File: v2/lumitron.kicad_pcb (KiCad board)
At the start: 2 copper layers, 40.6 x 78.7 mm, 11 parts

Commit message: track layout cleanup
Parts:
- moved BT2 1.40 mm to (101.6, 96.5)
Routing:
- net /f: track 46.0 -> 70.5 mm
- net /g: track 53.8 -> 67.1 mm
- net /d: track 13.5 -> 26.8 mm
- net /a: track 83.4 -> 91.3 mm
- net /b: track 70.9 -> 78.0 mm
- net /e: track 21.0 -> 18.4 mm
- net /c: track 27.2 -> 24.8 mm

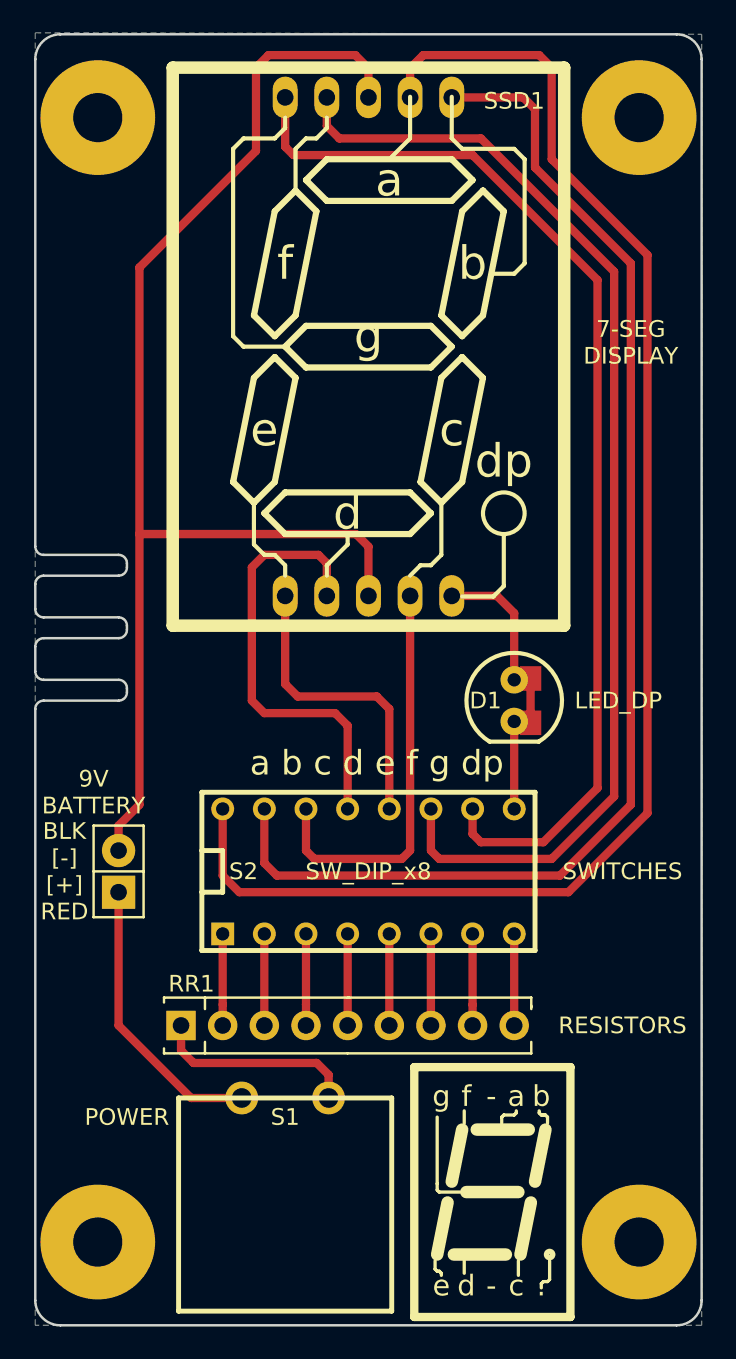
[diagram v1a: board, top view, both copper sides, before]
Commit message: added open source logo
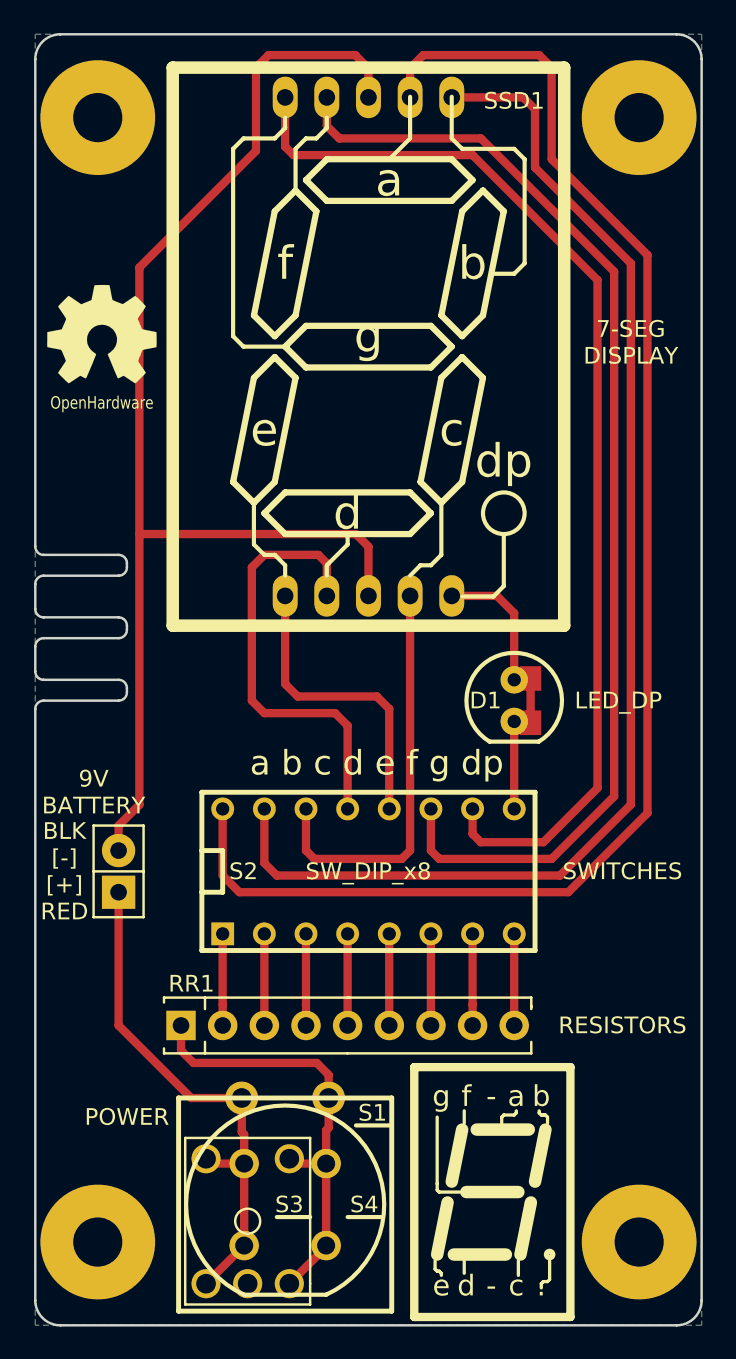
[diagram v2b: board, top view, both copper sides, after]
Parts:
- added G1: OSHW, lumitron_pcb:OSHW_6mm, F.Cu at (85.3, 94.5)
- added S3: POWER3, lumitron_pcb:sw_KSA_Tactile_SPST, F.Cu at (94.2, 148.6)
- added S4: POWER2, lumitron_pcb:sw_KS-01Q, F.Cu at (96.5, 147.6)
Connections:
- net Net-(RR1-Pad1) renamed /RES
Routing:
- net /[+]: track 17.5 -> 32.3 mm
- net /RES: track 12.6 -> 27.2 mm

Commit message: last cleanup before prototype
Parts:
- moved S3 0.25 mm to (94.2, 148.8)
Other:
- board text removed: "-"

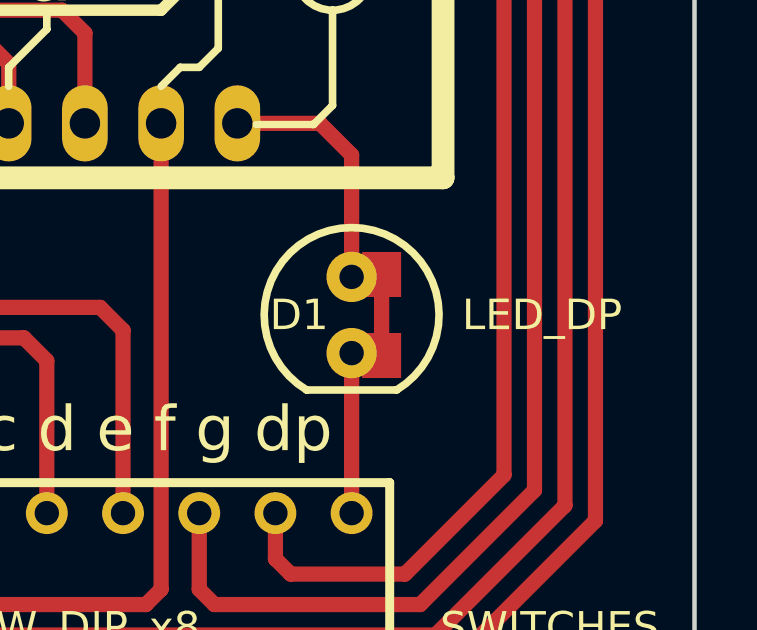
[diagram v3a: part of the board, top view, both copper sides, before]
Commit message: reverse LED DP D1 silk legend fixed
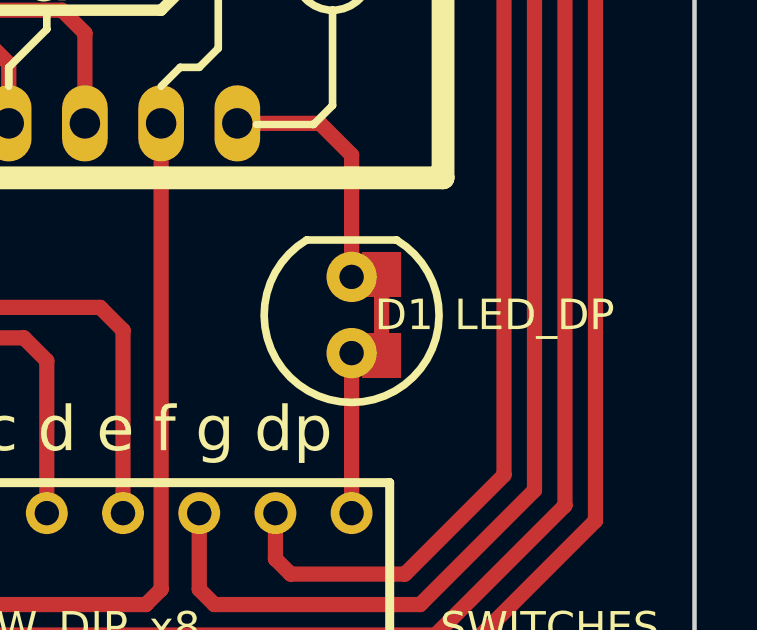
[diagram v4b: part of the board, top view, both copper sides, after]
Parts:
- turned D1 to 90 degrees
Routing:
- net /dp: track 18.4 -> 17.5 mm
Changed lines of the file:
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@@
     (thickness 1.6)
     (drawings 184)
-    (tracks 116)
+    (tracks 114)
     (zones 0)
     (modules 14)
@@
     (fp_text user [-] (at -10.16 1.27 180) (layer B.SilkS)
       (effects (font (size 1 1) (thickness 0.15)) (justify mirror))
-    )
-  )
-  (module lumitron_pcb:LED-5MM_SMD (layer F.Cu)
-    (at 110.49 116.84 270)
-    (descr "LED 5mm - Lead pitch 100mil (2,54mm)")
-    (tags "LED led 5mm 5MM 100mil 2,54mm")
-    (fp_text reference D1 (at 0 1.75 360) (layer F.SilkS)
-      (effects (font (size 1.016 1.016) (thickness 0.1524)))
-    )
-    (fp_text value LED_DP (at 0 -6.35 360) (layer F.SilkS)
-      (effects (font (size 1.016 1.016) (thickness 0.1524)))
-    )
-    (fp_arc (start 0 0) (end 2.5 1.5) (angle 298.0724869) (layer F.SilkS) (width 0.254))
-    (fp_line (start 2.5 -1.5) (end 2.5 1.5) (layer F.SilkS) (width 0.254))
-    (pad 1 thru_hole circle (at -1.27 0 270) (size 1.6764 1.6764) (drill 0.8128) (layers *.Cu *.Mask F.SilkS)
-      (net 9 /dp))
-    (pad 2 thru_hole circle (at 1.27 0 270) (size 1.6764 1.6764) (drill 0.8128) (layers *.Cu *.Mask F.SilkS)
-      (net 9 /dp))
-    (pad 1 smd rect (at -1.35 -1 270) (size 1.5 1.3) (layers F.Cu F.Paste F.Mask)
-      (net 9 /dp))
-    (pad 2 smd rect (at 1.35 -1 270) (size 1.5 1.3) (layers F.Cu F.Paste F.Mask)
-      (net 9 /dp))
-    (pad 1 smd rect (at -0.7 -1 270) (size 1.5 0.4) (layers F.Cu F.Paste F.Mask)
-      (net 9 /dp))
-    (pad 2 smd rect (at 0.7 -1 270) (size 1.5 0.4) (layers F.Cu F.Paste F.Mask)
-      (net 9 /dp))
-    (model LEDs/LED-5MM.wrl
-      (at (xyz 0 0 0))
-      (scale (xyz 1 1 1))
-      (rotate (xyz 0 0 0))
     )
   )
@@
     (pad 1 thru_hole circle (at -3.81 -2.54 90) (size 2 2) (drill 1.2) (layers *.Cu *.Mask F.SilkS)
       (net 17 /[+]))
+  )
+  (module lumitron_pcb:LED-5MM_SMD (layer F.Cu)
+    (at 110.49 116.84 90)
+    (descr "LED 5mm - Lead pitch 100mil (2,54mm)")
+    (tags "LED led 5mm 5MM 100mil 2,54mm")
+    (fp_text reference D1 (at 0 1.75 180) (layer F.SilkS)
+      (effects (font (size 1.016 1.016) (thickness 0.1524)))
+    )
+    (fp_text value LED_DP (at 0 6.096 180) (layer F.SilkS)
+      (effects (font (size 1.016 1.016) (thickness 0.1524)))
+    )
+    (fp_arc (start 0 0) (end 2.5 1.5) (angle 298.0724869) (layer F.SilkS) (width 0.254))
+    (fp_line (start 2.5 -1.5) (end 2.5 1.5) (layer F.SilkS) (width 0.254))
+    (pad 2 thru_hole circle (at -1.27 0 90) (size 1.6764 1.6764) (drill 0.8128) (layers *.Cu *.Mask F.SilkS)
+      (net 9 /dp))
+    (pad 1 thru_hole circle (at 1.27 0 90) (size 1.6764 1.6764) (drill 0.8128) (layers *.Cu *.Mask F.SilkS)
+      (net 9 /dp))
+    (pad 2 smd rect (at -1.35 1 90) (size 1.5 1.3) (layers F.Cu F.Paste F.Mask)
+      (net 9 /dp))
+    (pad 1 smd rect (at 1.35 1 90) (size 1.5 1.3) (layers F.Cu F.Paste F.Mask)
+      (net 9 /dp))
+    (pad 2 smd rect (at -0.7 1 90) (size 1.5 0.4) (layers F.Cu F.Paste F.Mask)
+      (net 9 /dp))
+    (pad 1 smd rect (at 0.7 1 90) (size 1.5 0.4) (layers F.Cu F.Paste F.Mask)
+      (net 9 /dp))
+    (model LEDs/LED-5MM.wrl
+      (at (xyz 0 0 0))
+      (scale (xyz 1 1 1))
+      (rotate (xyz 0 0 0))
+    )
   )
   (gr_line (start 99.06 153.67) (end 99.06 153.162) (layer F.SilkS) (width 0.2))
@@
   (segment (start 110.49 123.444) (end 110.49 122.456172) (width 0.508) (layer F.Cu) (net 9))
   (segment (start 110.49 122.456172) (end 110.49 118.11) (width 0.508) (layer F.Cu) (net 9))
-  (segment (start 110.49 115.57) (end 110.06 115.57) (width 0.508) (layer F.Cu) (net 9))
-  (segment (start 110.49 118.11) (end 110.06 118.11) (width 0.508) (layer F.Cu) (net 9))
   (segment (start 95.25 123.444) (end 95.25 126.746) (width 0.508) (layer F.Cu) (net 10))
   (segment (start 111.76 84.328) (end 111.76 80.772) (width 0.508) (layer F.Cu) (net 10))
